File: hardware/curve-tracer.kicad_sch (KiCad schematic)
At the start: 80 parts, among them J1 15V IN, J2 15V BENCH, J3 RANGE_FORCE, J4 RANGE_SENSE, J5 KELVIN HI / LO, J6 DUT G / D / S, J7 CN7 (morpho), J8 CN10 (morpho), Q1 BD139, Q2 MMBT3904, U1 OPA2197IDR, U2 OPA2197IDR, U3 OPA2197IDR

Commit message: Fix the Kelvin divider loading (F-1) and ADC clamp back-feed (F-2)
F-1: the Kelvin divider's current was counted as DUT current. Fixed
both ways.

- Hardware: divider 30k/10k -> 300k/100k 0.1% (Yageo RT0603, 25 ppm,
  C705762 / C122538, both in JLC stock). Ratio still /4; loading drops
  from 25 to 2.5 uA/V.
- Firmware: i_meas_ma is now DUT current, I_shunt - V_DS / CT_RDIV_OHM.
  CSV schema 1 -> 2, since the column's meaning changed. New header
  constants: cal_rdiv_ohm, cal_r_iso_ohm, and cal_r_ptc_ohm ("unset"
  until measured). The current limit acts on DUT current.
- Simulator: models the divider current through the shunt (--rdiv) and
  an optional PTC (--rptc), so the correction is exercised end to end.
  A build with the subtraction removed fails test_sweep: it reads 0.274
  vs 0.250 mA.
- Host: recompute applies the same subtraction (none for schema-1
  captures). New test_divider_correction.py shows the correction fires,
  and that an uncorrected 40 kohm sweep reads 36.4 kohm (40k || 400k).
- Blueprint §3.4: any resistive divider on the DUT node is counted as
  DUT current. DECISIONS.md records it as §13's phantom-current
  mechanism, reached by a different path.

Consequence, documented rather than hidden: on range 1 the term is
0.6 LSB at most, so an off device now reads within one LSB of zero on
either side, sometimes slightly negative. The sqrt(I) fit clamps at
zero; two tests that assumed exact zero / strict monotonicity now
allow one LSB.

F-2: R19/R22 51 ohm -> 1 kohm (C21190, Basic). Clamp current into
+3V3 is now ~11 mA per channel. Re-checked as asked:

- Leakage offset is up to 2 mV (BAT54S 2 uA max at 25 C), ~1 mV
  typical. It is not perfectly fixed, since it moves with signal and
  temperature; calibrate at zero, re-check at full scale.
- tau = 10 us against settle_us = 20 us: the first current conversion
  carries 5.9% of the step and the 64-sample mean 0.16% (~80 uA on the
  first point of each gate step on range 1). Voltage is sampled ~550 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
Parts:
- C1, D3, R23, R24, R4, R6, R8: Assembly (none) -> DNP
- C2, C3, C4, C5, C6, C7, C8, D1, D2, F1, NT1, NT2, R1, R10, R11, R12, R13, R14, R15, R16, R17, R18, R2, R3, R5, R7, R9, U1, U2, U3: Assembly (none) -> PCBA
- D4, D5: Assembly (none) -> PCBA; LCSC C19726 -> C7420333; MPN BAT54SLT1G -> BAT54S; Manufacturer onsemi -> R+O
- J1, J2, J3, J4, J5, J6, J7, J8, Q1, TP1, TP10, TP11, TP12, TP13, TP14, TP15, TP16, TP17, TP18, TP19, TP2, TP20, TP21, TP22, TP23, TP24, TP25, TP26, TP27, TP3, TP4, TP5, TP6, TP7, TP8, TP9: Assembly (none) -> hand
- Q2: Assembly (none) -> PCBA; LCSC C81464 -> C20526; MPN MMBT3904LT1G -> MMBT3904; Manufacturer onsemi -> JSCJ
- R19, R22: value 51 1% -> 1k 1%; Assembly (none) -> PCBA; LCSC C23197 -> C21190; MPN 0603WAF510JT5E -> 0603WAF1001T5E
- R20: value 30k 0.1% -> 300k 0.1%; footprint Resistor_SMD:R_0805_2012Metric -> Resistor_SMD:R_0603_1608Metric; Assembly (none) -> PCBA; LCSC C728649 -> C705762; MPN RT0805BRD0730KL -> RT0603BRD07300KL
- R21: value 10k 0.1% -> 100k 0.1%; footprint Resistor_SMD:R_0805_2012Metric -> Resistor_SMD:R_0603_1608Metric; Assembly (none) -> PCBA; LCSC C110775 -> C122538; MPN RT0805BRD0710KL -> RT0603BRD07100KL

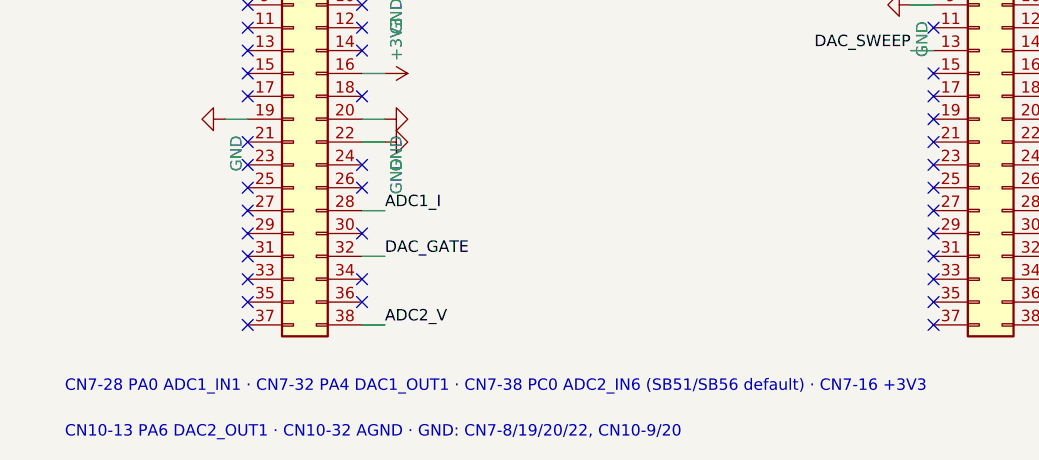
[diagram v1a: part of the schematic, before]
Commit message: hardware: H2 layout, routed and exported for the JLCPCB order
Pass 1 (analog-critical nets by hand) as approved, then Pass 2: board
shrunk to 135 x 92 mm, the remaining nets autorouted with Freerouting
v2.5.0 over the locked Pass 1 copper (DECISIONS.md P-5..P-10). DRC with
schematic parity, ERC and check_topology.py --self-test are clean.

- J7/J8 use a project footprint with mirrored pad numbering (L-2); its 3D
  model is shifted one pitch so the renders show the socket on its pads.
- DECISIONS.md: the split-crossing distances to NT2 and why the feedback
  tap crossing is not a 3 MHz stability term (P-1), the JLCPCB quotes and
  why 100 x 100 is not reachable (P-5), the Q1 thermal estimate (P-8),
  the CPL rotation sources (P-10), and the analyzer and lifecycle triage.
- tools/export_fab.py writes the Gerbers, drill, JLC BOM (hand-solder lines
  marked, no LCSC number) and JLC CPL, and refuses to write them if the
  BOM and CPL disagree.
- README: Freerouting in the toolchain, fab outputs, and a pre-order
  footprint-orientation check for the parts no automated check can see.
- review/: Pass 1 and Pass 2 renders and metrics, for the README and the
  write-up's design decisions.

Co-Authored-By: Claude Opus 5.5 <noreply@anthropic.com>
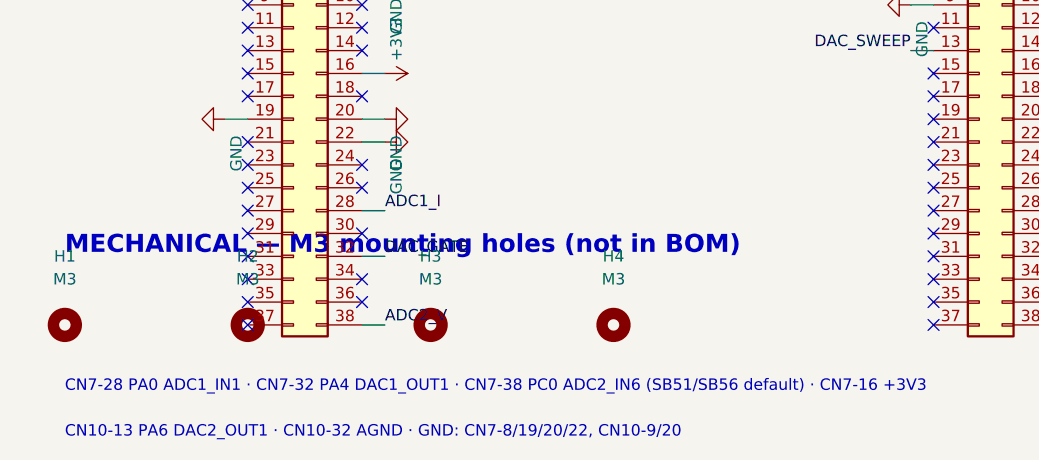
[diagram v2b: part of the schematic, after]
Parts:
- added H1, H2, H3, H4: M3, MountingHole:MountingHole_3.2mm_M3, symbol Mechanical:MountingHole
- J7, J8: footprint Connector_PinSocket_2.54mm:PinSocket_2x19_P2.54mm_Vertical -> curve-tracer:PinSocket_2x19_P2.54mm_Vertical_NucleoCarrier
- NT1, NT2: Assembly PCBA -> none; now left out of the parts list
- TP6: Assembly hand -> none; now left out of the parts list
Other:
- note added: "MECHANICAL — M3 mounting holes (not in BOM)"

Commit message: hardware: J1 reverse-polarity P-FET, heatsink rule, NT2 justified
- Q3 HL2303 (JLC Preferred, -30 V, +/-20 V gate, <= 28.5 mV at 150 mA) in
  the high side of J1, with D6 (12 V gate-source clamp, D2's line) and R25
  (10k gate pull-down, Basic): no new loading fee. Placed in the free patch
  above J1; the +15V pour's left edge moves from x 12 to 17. No existing
  copper removed or moved, no Pass 1 copper involved. TP28 bare pad on VIN.
- check_topology.py asserts the protection and plants two new faults
  (drain/source swapped, gate Zener reversed): 55/55, 11/11 caught.
- DECISIONS.md: P-11 records the part choice and that the 9.06 V headroom
  is set downstream of the loop, so a Schottky would not have touched it;
  P-12 no EMI filter and why; P-13 no fiducials; NT2 stays, on the
  crossing numbers. J2 is not behind Q3 and is flagged.
- The heatsink is required for any short test: stated in README.md, an
  H4 verified item (tab isolation, case temperature), and silkscreen
  inside the keep-out where the heatsink covers it.
- Re-exported: ERC, DRC with schematic parity, and the checker are clean.

Co-Authored-By: Claude Opus 5.5 <noreply@anthropic.com>
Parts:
- added D6: BZT52C12 12V, Diode_SMD:D_SOD-123, symbol Device:D_Zener
- added Q3: HL2303, Package_TO_SOT_SMD:SOT-23, symbol Transistor_FET:Q_PMOS_GSD
- added R25: 10k 1%, Resistor_SMD:R_0603_1608Metric, symbol Device:R
- added TP28: VIN (pad), TestPoint:TestPoint_Pad_D1.0mm, symbol Connector:TestPoint
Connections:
- net +15V: now also D6.1 (K), Q3.2 (S); no longer J1.1
- net GNDPWR: now also R25.2
- new net RP_GATE: D6.2 (A), Q3.1 (G), R25.1
- new net VIN: J1.1, Q3.3 (D), TP28.1
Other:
- note added: "Q3/D6/R25: J1 reverse-polarity protection. Drain to the jack, source to +15V. J2 is not behind it."
- note added: "TP28 is a bare SMD pad for want of room by J1: VIN against TP7 (+15V) is Q3's drop."

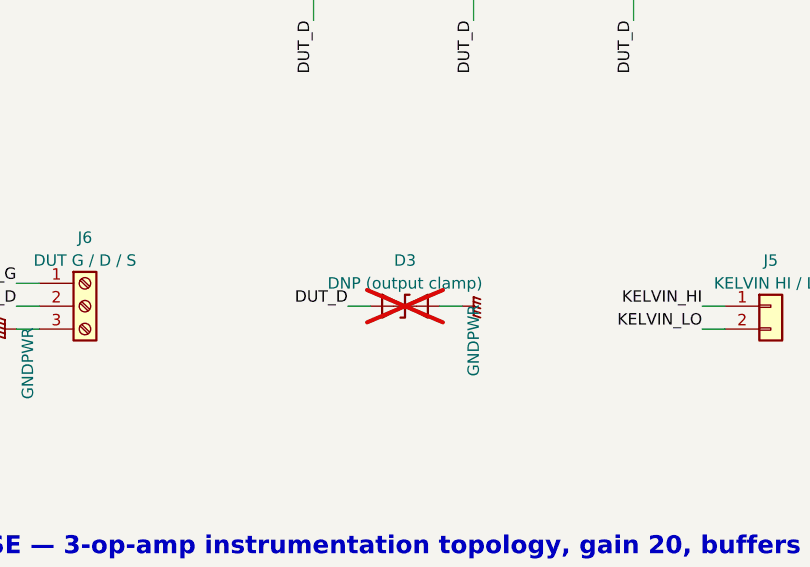
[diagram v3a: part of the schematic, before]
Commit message: Step 15 threshold 16 V; DUT-node design rule; D3 part number in schematic
- H4 step 15: pass <= 16.0 V (was 12.0 V). With D3 fitted, 13.3-14.8 V is
  the SMAJ12A working as specified; above 16 V is something other than the
  structural overshoot sim 10 predicts. D3 bounds a microsecond transient,
  not the 10 V ceiling; sustained overcurrent is the firmware limit's job.
  The scope is now centred at +10 V so a 16 V peak is on screen.
- Blueprint 3.3: everything on the DUT node is read as DUT current, with
  three instances (13's bridge, F-1's divider, D3's leakage). Anything
  added there is checked against range 3. 3.4 and F-1 point to it.
- D3 schematic and PCB fields: SMAJ12A, MDD, C113957, still DNP. Fields
  only; DRC with parity, ERC and the topology checker are clean.

Co-Authored-By: Claude Opus 5.5 <noreply@anthropic.com>
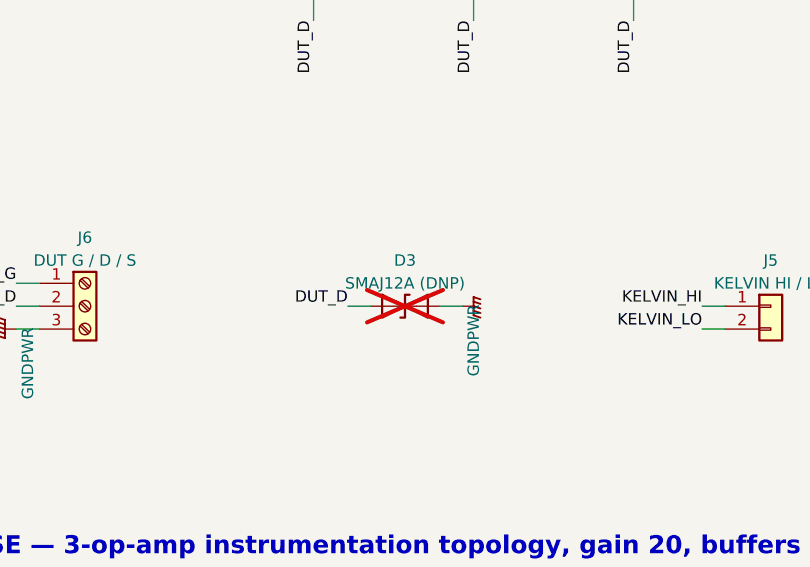
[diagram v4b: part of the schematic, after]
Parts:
- D3: value DNP (output clamp) -> SMAJ12A (DNP); LCSC (none) -> C113957; MPN (none) -> SMAJ12A; Manufacturer (none) -> MDD(Microdiode Semiconductor)
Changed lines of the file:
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@@
 			)
 		)
-		(property "Value" "DNP (output clamp)"
+		(property "Value" "SMAJ12A (DNP)"
 			(at 304.8 86.36 0)
 			(show_name no)
@@
 			)
 		)
-		(property "Description" "Output clamp footprint at DUT socket (§14.6)"
+		(property "Description" "Output clamp TVS at DUT socket; fit only if H4 step 15 fails (blueprint §3.6)"
 			(at 304.8 88.9 0)
 			(hide yes)
@@
 			)
 		)
-		(property "MPN" ""
+		(property "MPN" "SMAJ12A"
 			(at 304.8 88.9 0)
 			(hide yes)
@@
 			)
 		)
-		(property "Manufacturer" ""
+		(property "Manufacturer" "MDD(Microdiode Semiconductor)"
 			(at 304.8 88.9 0)
 			(hide yes)
@@
 			)
 		)
-		(property "LCSC" ""
+		(property "LCSC" "C113957"
 			(at 304.8 88.9 0)
 			(hide yes)

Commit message: Fit D3 by default; step 15 verifies, step 13a tells D3 from no D3
- D3 SMAJ12A moves from DNP to PCBA: schematic, PCB, engineering BOM, JLC
  BOM and CPL (26 lines, 39 rows; +1 extended line, $54 in fees). Symbol
  is now Diode:SMAJ12A (unidirectional) instead of the bidirectional
  Device:D_TVS; pin 1, the cathode, stays on DUT_D. Gerbers unchanged.
- DECISIONS D3 records the trade: <= 1 uA on the DUT node, 10% of range 3
  full scale and negligible on range 1, with ranges 2-3 outside the MVP,
  against bounding the overshoot sim 10 predicts on every limit release.
- H4 step 15 is now a verification: expect 13.3-14.8 V, pass <= 16 V. It
  cannot confirm D3 on its own (the unclamped peak is also ~14.8 V), so new
  step 13a drives D3 into DC breakdown through 10 k from +15 V with J3 and
  the Kelvin pair off: 12.0-14.8 V means fitted and the right way round.
- check_topology: D3 polarity and fitted; the DUT-node parts list is
  fixed (blueprint 3.3). 59/59, 14 planted faults caught.
- C1, R4, R6, R8 values and descriptions filled, still DNP; C1 and R8 have
  MPN and LCSC. R4/R6 are on-hand generic parts with no MPN.

Co-Authored-By: Claude Opus 5.5 <noreply@anthropic.com>
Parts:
- C1: value DNP (C_f) -> 3.3p C0G (DNP); LCSC (none) -> C2836771; MPN (none) -> 0603CG3R3B500NT; Manufacturer (none) -> FH (Guangdong Fenghua)
- D3: value SMAJ12A (DNP) -> SMAJ12A; symbol Device:D_TVS -> Diode:SMAJ12A; Assembly DNP -> PCBA; now fitted
- R4: value DNP (R_B alt) -> 330 1% (DNP)
- R6: value DNP (R_sense alt) -> 10 1% (DNP)
- R8: value DNP (R_iso alt) -> 47 1% 1W (DNP); LCSC (none) -> C385394; MPN (none) -> RN1WS47ΩFT/BA1; Manufacturer (none) -> TyoHM
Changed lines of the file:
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@@
 			)
 		)
-		(property "Value" "DNP (C_f)"
+		(property "Value" "3.3p C0G (DNP)"
 			(at 116.84 52.07 0)
 			(show_name no)
@@
 			)
 		)
-		(property "Description" "C_f across R_f"
+		(property "Description" "C_f across R_f. 3.3 pF hand-fitted at H4 P3; the C_f sweep may change it (CONTINGENCY.md §2)"
 			(at 114.3 50.8 0)
 			(hide yes)
@@
 			)
 		)
-		(property "MPN" ""
+		(property "MPN" "0603CG3R3B500NT"
 			(at 114.3 50.8 0)
 			(hide yes)
@@
 			)
 		)
-		(property "Manufacturer" ""
+		(property "Manufacturer" "FH (Guangdong Fenghua)"
 			(at 114.3 50.8 0)
 			(hide yes)
@@
 			)
 		)
-		(property "LCSC" ""
+		(property "LCSC" "C2836771"
 			(at 114.3 50.8 0)
 			(hide yes)
@@
 			)
 		)
-		(property "Value" "DNP (R_B alt)"
+		(property "Value" "330 1% (DNP)"
 			(at 50.8 90.17 0)
 			(show_name no)
@@
 			)
 		)
-		(property "Description" "R_B alternate-value footprint"
+		(property "Description" "R_B alternate. 330 ohm axial IN PARALLEL with R3 = 165 ohm (CONTINGENCY.md A5). On hand, blueprint §8: no MPN"
 			(at 48.26 88.9 0)
 			(hide yes)
@@
 	)
 	(symbol
-		(lib_id "Device:D_TVS")
+		(lib_id "Diode:SMAJ12A")
 		(at 304.8 88.9 0)
 		(unit 1)
@@
 		(on_board yes)
 		(in_pos_files yes)
-		(dnp yes)
+		(dnp no)
 		(property "Reference" "D3"
 			(at 304.8 83.82 0)
@@
 			)
 		)
-		(property "Value" "SMAJ12A (DNP)"
+		(property "Value" "SMAJ12A"
 			(at 304.8 86.36 0)
 			(show_name no)
@@
 			)
 		)
-		(property "Description" "Output clamp TVS at DUT socket; fit only if H4 step 15 fails (blueprint §3.6)"
+		(property "Description" "Output clamp TVS at DUT socket, fitted (blueprint §3.6)"
 			(at 304.8 88.9 0)
 			(hide yes)
@@
 			)
 		)
-		(property "Assembly" "DNP"
+		(property "Assembly" "PCBA"
 			(at 304.8 88.9 0)
 			(hide yes)
@@
 			)
 		)
-		(property "Value" "DNP (R_sense alt)"
+		(property "Value" "10 1% (DNP)"
 			(at 53.34 123.19 0)
 			(show_name no)
@@
 			)
 		)
-		(property "Description" "R_sense alternate-value footprint"
+		(property "Description" "R_sense alternate. 10 ohm axial IN PARALLEL with R5 = 5 ohm, only for a trip that reads low (CONTINGENCY.md §4). On hand, blueprint §8: no MPN"
 			(at 50.8 121.92 0)
 			(hide yes)
@@
 			)
 		)
-		(property "Value" "DNP (R_iso alt)"
+		(property "Value" "47 1% 1W (DNP)"
 			(at 104.14 123.19 0)
 			(show_name no)
@@
 			)
 		)
-		(property "Description" "R_iso alternate-value footprint"
+		(property "Description" "R_iso alternate. 47 ohm fitted ALONE, R7 removed first; in parallel it lowers R_iso (CONTINGENCY.md A6)"
 			(at 101.6 121.92 0)
 			(hide yes)
@@
 			)
 		)
-		(property "MPN" ""
+		(property "MPN" "RN1WS47ΩFT/BA1"
 			(at 101.6 121.92 0)
 			(hide yes)
@@
 			)
 		)
-		(property "Manufacturer" ""
+		(property "Manufacturer" "TyoHM"
 			(at 101.6 121.92 0)
 			(hide yes)
@@
 			)
 		)
-		(property "LCSC" ""
+		(property "LCSC" "C385394"
 			(at 101.6 121.92 0)
 			(hide yes)

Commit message: Zero hand-soldering: through-hole parts to PCBA, test loops dropped, ORDER.md
- J1-J8 and Q1 back on the PCBA order. Each checked in JLCPCB's part
  record: THT, manualWeld, available. export_fab.py checks through-hole
  PCBA parts against THT_VERIFIED instead of refusing them, and writes one
  JLC BOM line per LCSC part: 32 lines, 48 CPL rows, no hand-solder lines.
- TP1-TP27: no loops. Bare 1.0 mm plated holes, out of the BOM and CPL.
  H4 card: scope probe in a holder with its ground on J2 GND (the old
  "spring ground on TP27" was 50 mm from TP3); 13a clips moved to the
  supply post and J6. CONTINGENCY A2 changes the ground path instead.
- Heatsink: Boyd 577500B00000G (26 C/W, fits the keep-out); step 14d
  expects ~48 C.
- ORDER.md: JLCPCB $174.52 for 5 assembled boards (2 assembled: $153.33),
  LCSC $11.66 incl. shunts, DigiKey $3.52, plus a verify list.
- DECISIONS records the reversal, its cost ($18.42 in fees for six
  parts), and that Keystone 5001 is in JLCPCB's library after all.

Co-Authored-By: Claude Opus 5.5 <noreply@anthropic.com>
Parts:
- J1, J2, J3, J4, J5, J6, J7, J8, Q1: Assembly hand -> PCBA
- TP1, TP10, TP11, TP12, TP13, TP14, TP15, TP16, TP17, TP18, TP19, TP2, TP20, TP21, TP22, TP23, TP24, TP25, TP26, TP27, TP3, TP4, TP5, TP7, TP8, TP9: Assembly hand -> none; MPN 5001 -> (none); Manufacturer Keystone -> (none); now left out of the parts list

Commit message: Test loops back as JLC-assembled RH-5001; all 5 boards assembled; R2-1
- TP1-TP27 (not TP6): RH-5001 (ronghe, C5199801), PCBA, THT/manualWeld,
  in the unchanged Keystone 5001 footprint. Added to THT_VERIFIED. JLC BOM
  33 lines, CPL 74 rows.
- H4 card and CONTINGENCY back to clip leads on loops (13a on TP7/TP19, no
  probe holder). Kept: the scope ground is a clip lead on TP27, not a
  spring ground; A2 moves that lead to TP9. Heatsink part and 14d kept.
- All 5 boards assembled. ORDER.md: JLCPCB $188.88 (loops $14.36; 5 vs 2
  assembled is now $27.80), LCSC $11.66, DigiKey $3.52.
- DECISIONS: TP row, assembly record, and rev-2 item R2-1: no safe scope
  spring-ground point near TP3; rev 2 adds a ground pad or via within a
  few mm of it.

Co-Authored-By: Claude Opus 5.5 <noreply@anthropic.com>
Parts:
- TP1, TP10, TP11, TP12, TP13, TP14, TP15, TP16, TP17, TP18, TP19, TP2, TP20, TP21, TP22, TP23, TP24, TP25, TP26, TP27, TP3, TP4, TP5, TP7, TP8, TP9: Assembly none -> PCBA; LCSC (none) -> C5199801; MPN (none) -> RH-5001; Manufacturer (none) -> ronghe; now in the parts list

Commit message: C5 to C47023118; CPL: no correction by analogy, THT at body centre
- C5: ROQANG C72487 is "Standard Only" at JLCPCB, so it is replaced by
  jieerrui RVT50V10M5X5 (C47023118): same RVT series, 2000 h at 105 C,
  17 mA at 120 Hz. No ESR is listed for either part, so ESR, the parameter
  that matters for damping the supply lead, is inferred.
- CPL: the +180 on CP_Elec (taken by analogy) is removed; JLCPCB's preview
  drew C5 reversed with it. Through-hole parts are placed at their F.Fab
  body centre, not pin 1, and TO-126 / 2.54 mm headers and sockets get +90,
  read off JLCPCB's preview. export_fab.py now needs KiCad's Python.
- ORDER.md: JLCPCB $188.56. DECISIONS C5 and P-10 record both changes.

Co-Authored-By: Claude Opus 5.5 <noreply@anthropic.com>
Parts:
- C5: LCSC C72487 -> C47023118; MPN RVT1H100M0505 -> RVT50V10M5X5; Manufacturer ROQANG -> jieerrui
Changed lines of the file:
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@@
 			)
 		)
-		(property "MPN" "RVT1H100M0505"
+		(property "MPN" "RVT50V10M5X5"
 			(at 81.28 243.84 0)
 			(hide yes)
@@
 			)
 		)
-		(property "Manufacturer" "ROQANG"
+		(property "Manufacturer" "jieerrui"
 			(at 81.28 243.84 0)
 			(hide yes)
@@
 			)
 		)
-		(property "LCSC" "C72487"
+		(property "LCSC" "C47023118"
 			(at 81.28 243.84 0)
 			(hide yes)
